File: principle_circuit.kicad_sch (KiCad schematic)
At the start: 10 parts, among them Q1 NMOS, Q2 PMOS, U1 OPA2156xD, U2 OPA2156xD, U3 up to 1.5kV

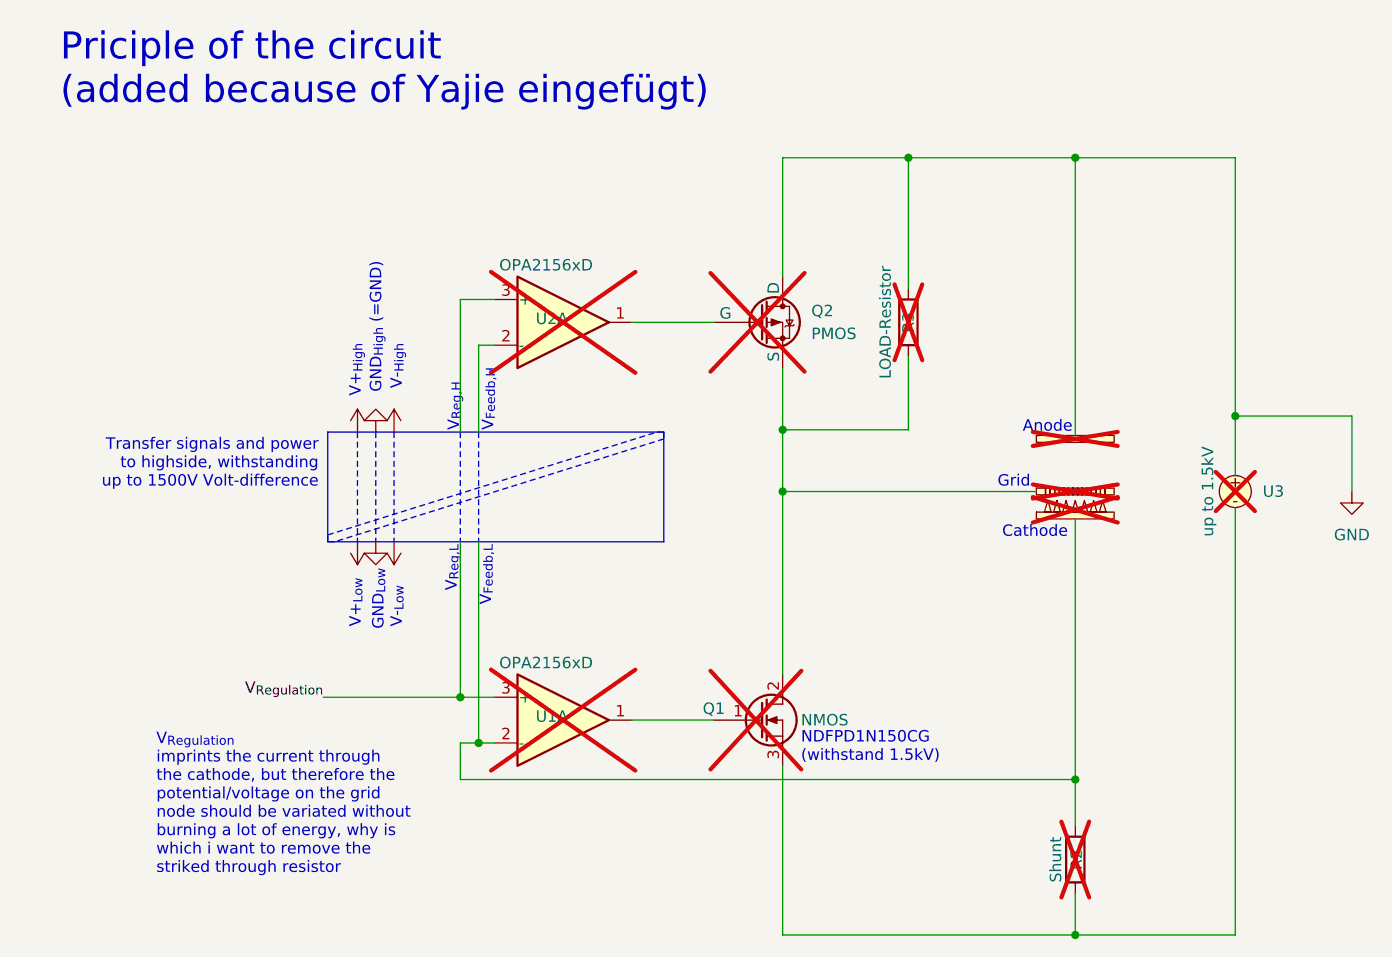
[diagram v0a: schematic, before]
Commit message: Added option to invert FET-Gate voltage
Added JP206 (3Pad Solder Jumper) and JP204 (2Pad Solder Jumper)
These using the, until now, unused second OpAmp of U201.

--> Jumpers that allow to invert the FET-Gate Voltage

FET-Gate Voltage acts as Grid-Regulation (inverting):
- Close JP206 Pins 2 with 3
- Close JP204
- Use R215 = 1Meg

FET-Gate Voltage acts as Cath-Regulation (non inverting):
- Close JP206 Pins 2 with 1
- Open  JP204
- Use R215 = 0R (Short-Circuit)

Candidate for V1.2
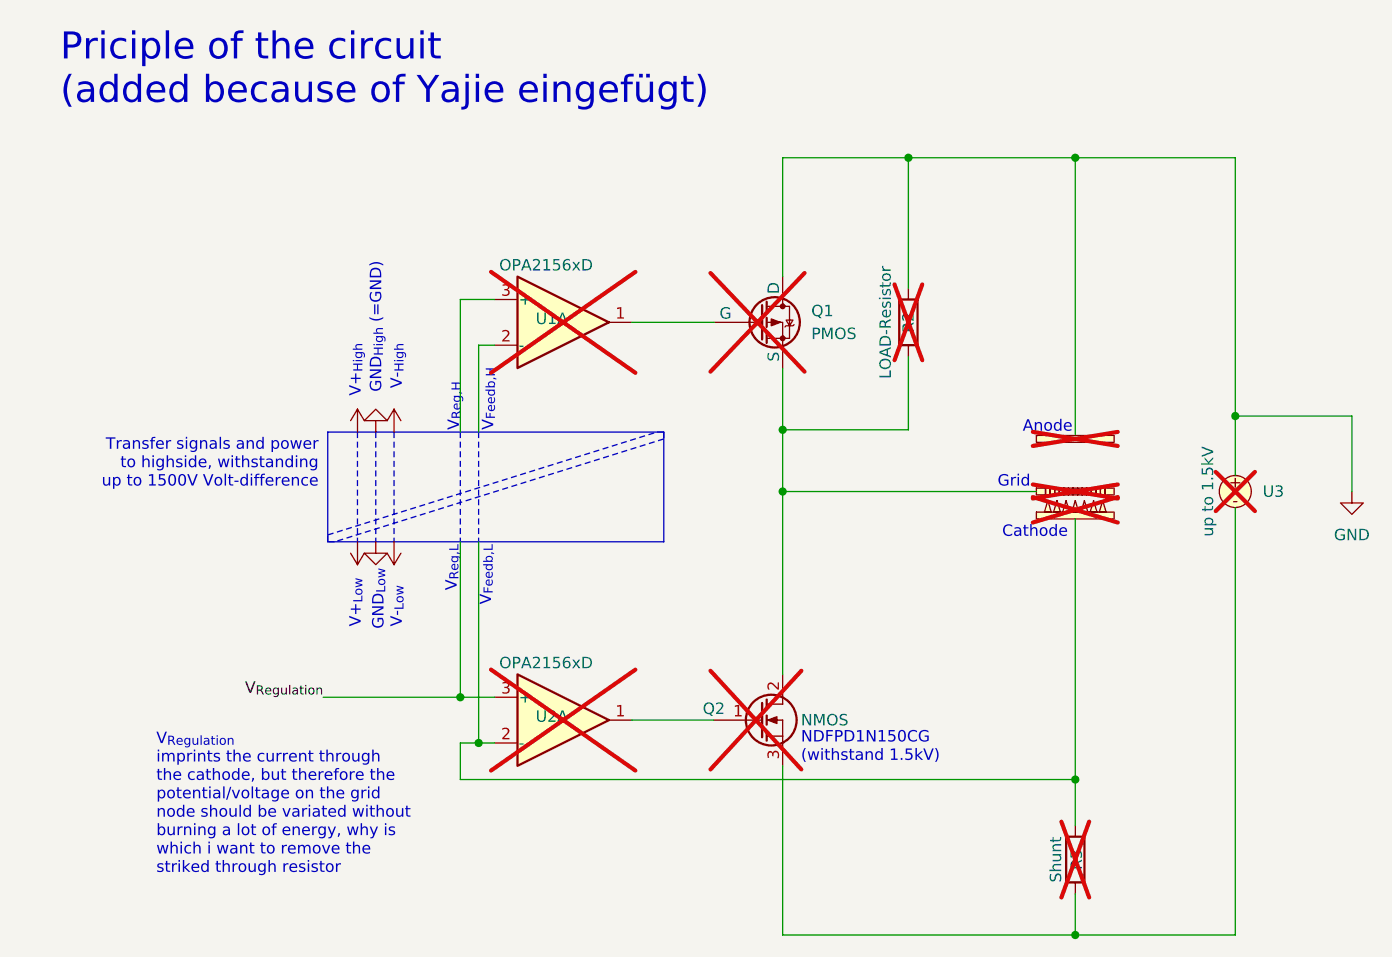
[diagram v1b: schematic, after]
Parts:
- renumbered Q2 to Q1, Q1 to Q2, R3 to R2, R2 to R3, U2 to U1, U1 to U2
